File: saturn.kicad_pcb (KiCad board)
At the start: 4 copper layers, 100 x 66 mm, 101 parts, among them J1 Conn_01x04_Pin, J10 Conn_01x04, J11 USB_B_Micro, J12 USB_C_Receptacle_USB2.0, J13 ZX-XH2.54-3PWT, J14 Conn_01x04_Pin, J2 PMOD3_FULL, J3 Conn_01x06, J4 Conn_01x06, J6 ZX-XH2.54-10PWT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

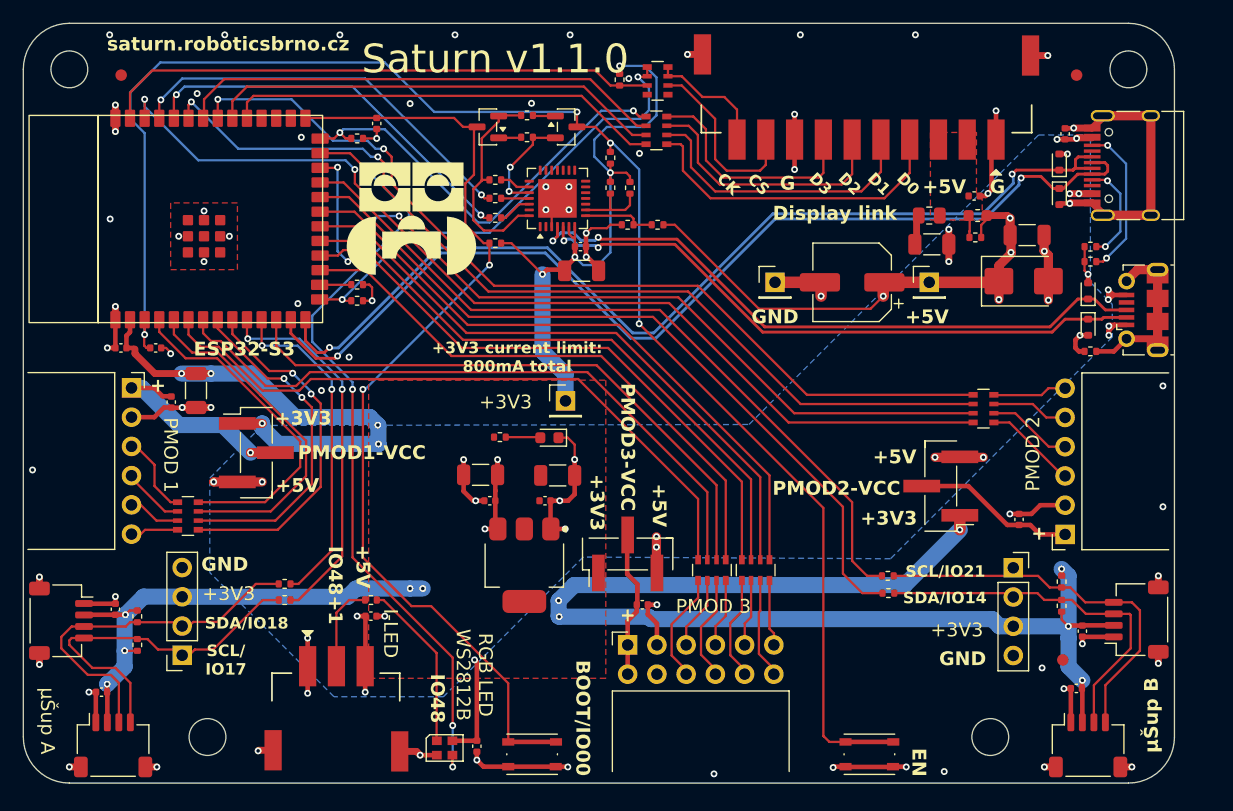
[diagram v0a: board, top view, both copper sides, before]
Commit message: Tune silkscreen, enlarge SMT switch pads
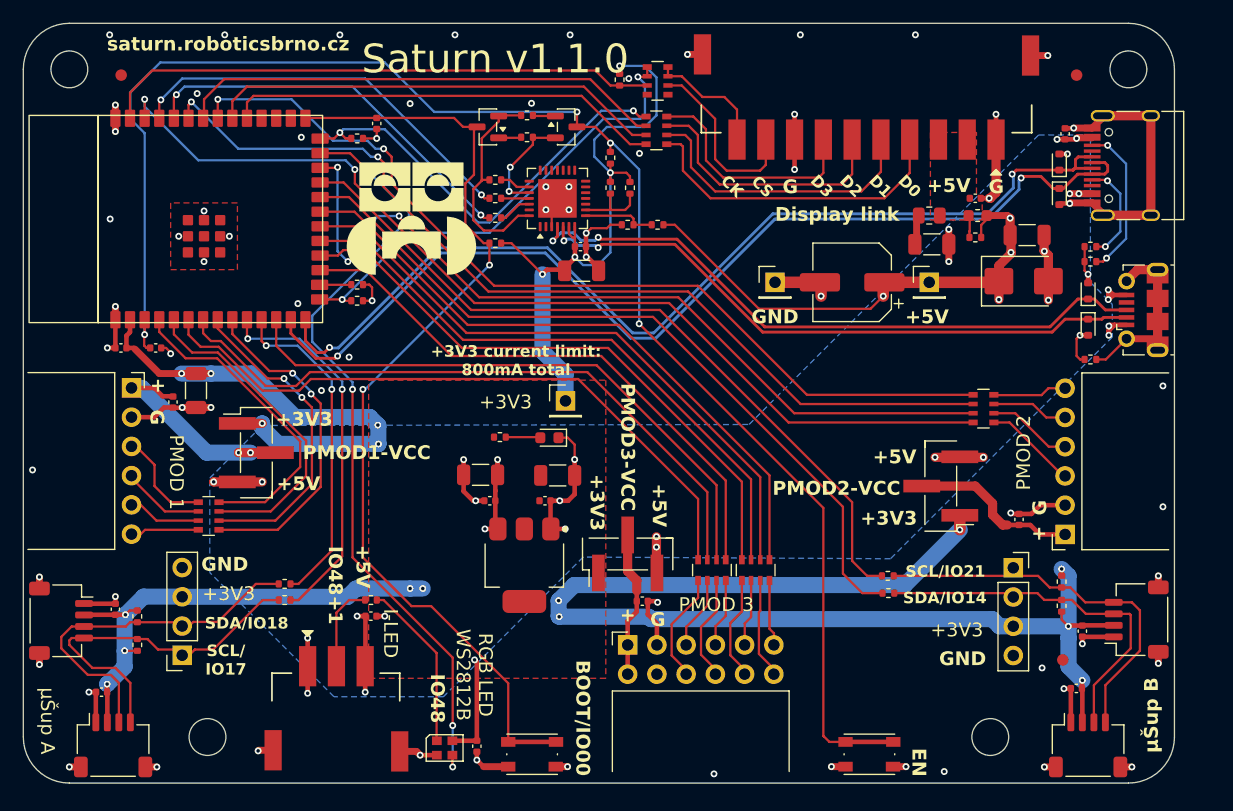
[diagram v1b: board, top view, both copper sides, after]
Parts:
- SW2, SW3: footprint Button_Switch_SMD:SW_Push_1P1T_NO_Vertical_Wuerth_434133025816 -> Switch_SMT:SW_SMD_LargePads
- moved RN1 1.80 mm to (61.1, 98.8)
- moved R71 0.70 mm to (137.7, 85.2)
- moved C9 0.31 mm to (98.8, 106.2)
- moved C21 0.22 mm to (127.7, 71.2)
- moved C23 0.15 mm to (58.0, 88.9)
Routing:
- net GND: track 168.3 -> 161.1 mm
- net Net-(J3-Pin_3): track 5.41 -> 7.21 mm
- net Net-(J3-Pin_2): track 4.57 -> 6.37 mm
- net Net-(J3-Pin_1): track 4.16 -> 5.96 mm
- net Net-(J3-Pin_4): track 7.09 -> 8.89 mm
- net /PMOD1_IO2: track 29.7 -> 27.9 mm
- net /PMOD1_IO1: track 30.9 -> 29.1 mm
- net /PMOD1_IO4: track 29.6 -> 27.8 mm
- net /PMOD1_IO3: track 30.3 -> 28.5 mm
- net Net-(J3-Pin_6): track 18.6 -> 19.8 mm, vias 1 -> 2
- net Net-(J4-Pin_6): track 14.2 -> 14.8 mm
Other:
- board text added: "ESP32-S3-WROOM-1-N16R8 Octal PSRAM"
- board text removed: "ESP32-S3"

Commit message: Use 0805 10u capacitors (cheaper)
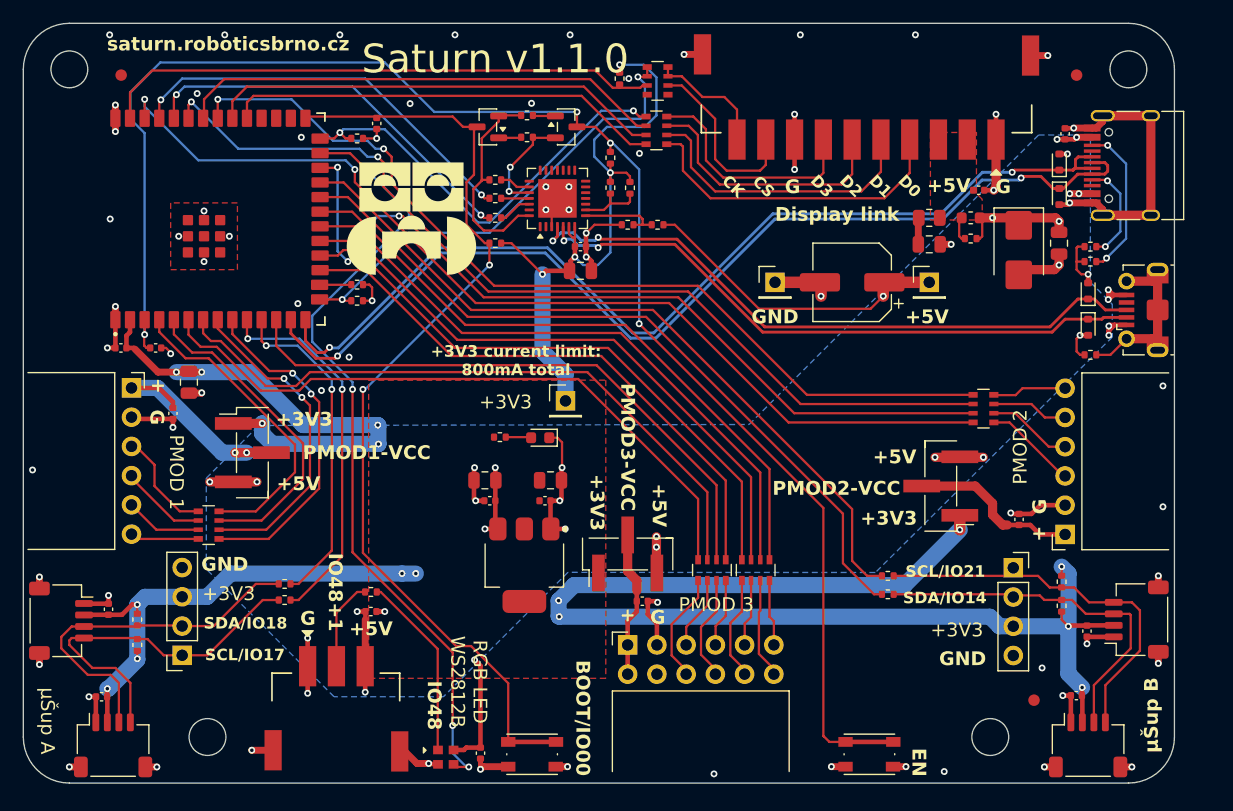
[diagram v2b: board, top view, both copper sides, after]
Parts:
- C1, C24, C3, C4, C5, C6: footprint Capacitor_SMD:C_1206_3216Metric -> Capacitor_SMD:C_0805_2012Metric
- J11: footprint Connector_USB:USB_Micro-B_Molex-105017-0001 -> USB_Conn:USB_Micro-B_XNJ-073_With_THR_Paste
- J12: footprint Connector_USB:USB_C_Receptacle_HRO_TYPE-C-31-M-12 -> USB_Conn:USB_C_Receptacle_HRO_TYPE-C-31-M-12_With_THR_Paste
- U1: footprint RKL-ESP:ESP32-S3-WROOM -> ESP32-WROOM:ESP32-S3-WROOM
- U9: footprint LED_SMD:LED_WS2812B-2020_PLCC4_2.0x2.0mm -> XL-2020RGBC-WS2812B:LED_WS2812B-2020_PLCC4_2.0x2.0mm
- moved FID3 4.30 mm to (132.8, 114.8)
- moved C4 2.86 mm to (135.0, 75.1), turned to -90 degrees
- moved D5 2.73 mm to (131.5, 75.7), turned to -90 degrees
- moved C23 0.99 mm to (58.0, 89.9)
- moved C1 0.95 mm to (59.4, 87.2)
- moved U9 0.81 mm to (81.7, 119.8)
- moved D2 0.80 mm to (89.9, 92.0)
- moved RN1 0.79 mm to (61.1, 99.6)
- moved C21 0.76 mm to (128.0, 70.5)
- moved C5 0.75 mm to (90.8, 95.7)
- moved R33 0.70 mm to (75.2, 105.4)
- moved C16 0.68 mm to (84.7, 119.4)
- moved FB1 0.63 mm to (127.3, 72.9)
- moved C13 0.62 mm to (136.5, 114.4)
- moved C6 0.61 mm to (85.1, 95.7)
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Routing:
- net +5V: track 89.8 -> 83.4 mm, vias 21 -> 20
- net GND: track 161.1 -> 155.3 mm, vias 88 -> 86
- net Net-(U9-DOUT): track 14.7 -> 16.4 mm
- net +3V3: track 248.4 -> 249.8 mm
- net /SMART_LEDS: track 67.6 -> 68.7 mm
- net Net-(J11-Shield): track 16.3 -> 15.4 mm
- net /I2CB_SDA: track 66.5 -> 65.6 mm
- net /USBMAIN_D+: track 86.8 -> 85.9 mm
- net Net-(D2-A): track 3.02 -> 2.22 mm
- net Net-(U3-VBUS): track 6.38 -> 7.15 mm
- net Net-(U3-~{RST}): track 6.44 -> 5.71 mm
- net Net-(J3-Pin_6): track 19.8 -> 20.4 mm
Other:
- board text removed: "SCL/ IO17"

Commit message: Use AMS1117-3.3 LDO (cheaper)
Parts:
- U2: value SGM2212-3.3XKC3G -> AMS1117-3.3
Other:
- board text added: "+3V3 current limit: 1A total"
- board text removed: "+3V3 current limit: 800mA total"
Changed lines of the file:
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@@
 			)
 		)
-		(property "Value" "SGM2212-3.3XKC3G"
+		(property "Value" "AMS1117-3.3"
 			(at 0.0625 -6.25 90)
 			(layer "F.Fab")
@@
 			)
 		)
-		(property "LCSC" "C3294699"
+		(property "LCSC" "C6186"
 			(at 0 0 270)
 			(unlocked yes)
@@
 		(layer "Edge.Cuts")
 	)
-	(gr_text "+3V3 current limit:\n800mA total"
+	(gr_text "+3V3 current limit:\n1A total"
 		(at 87.8 85.3 0)
 		(layer "F.SilkS")
@@
 	)
 	(gr_text "Display link"
-		(at 115.7 72.6 0)
+		(at 115.6 72.9 0)
 		(layer "F.SilkS")
 		(effects

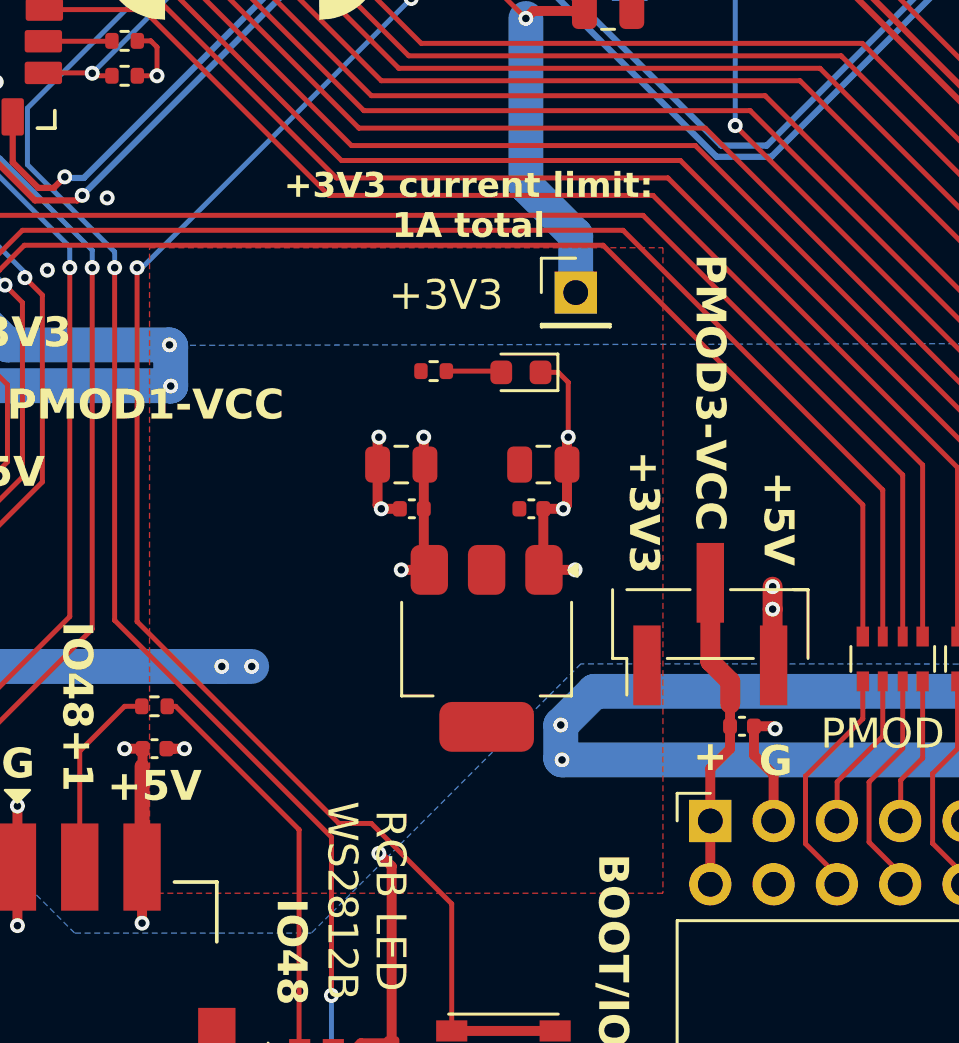
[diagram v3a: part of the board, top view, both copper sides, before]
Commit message: Add LDO output cap series resistance
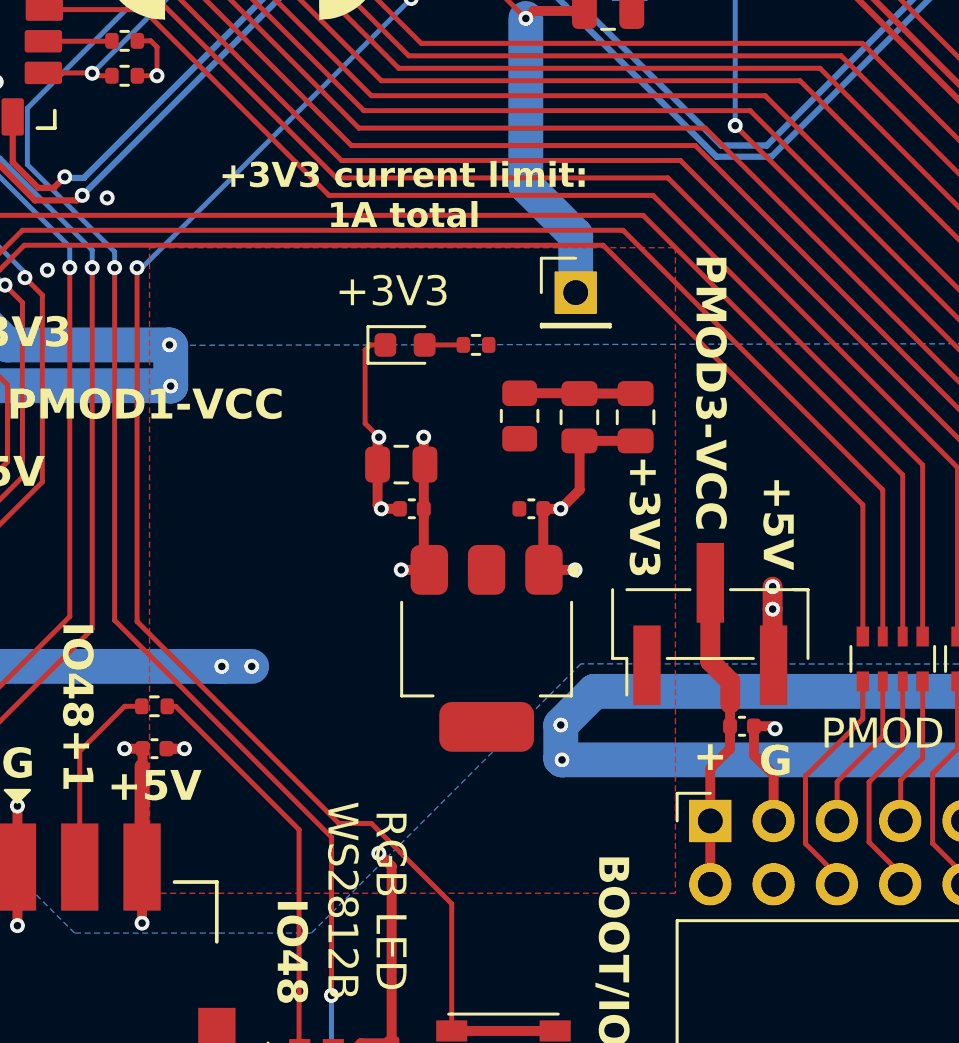
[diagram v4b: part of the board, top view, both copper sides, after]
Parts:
- added C25: 10u, Capacitor_SMD:C_0805_2012Metric, F.Cu at (94.5, 93.8)
- added R20: 4R7, Resistor_SMD:R_0805_2012Metric, F.Cu at (89.8, 93.8)
- moved D2 4.78 mm to (85.2, 90.9), turned to 0 degrees
- moved C5 2.39 mm to (92.2, 93.8), turned to -90 degrees
- moved R5 2.00 mm to (88.1, 90.9), turned to 180 degrees
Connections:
- C5 pad 1: +3V3 -> Net-(C25-Pad1)
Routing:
- net Net-(C25-Pad1): track 0.00 -> 4.66 mm
- net GND: track 155.3 -> 158.7 mm, vias 86 -> 85
- net Net-(D2-A): track 2.22 -> 1.55 mm

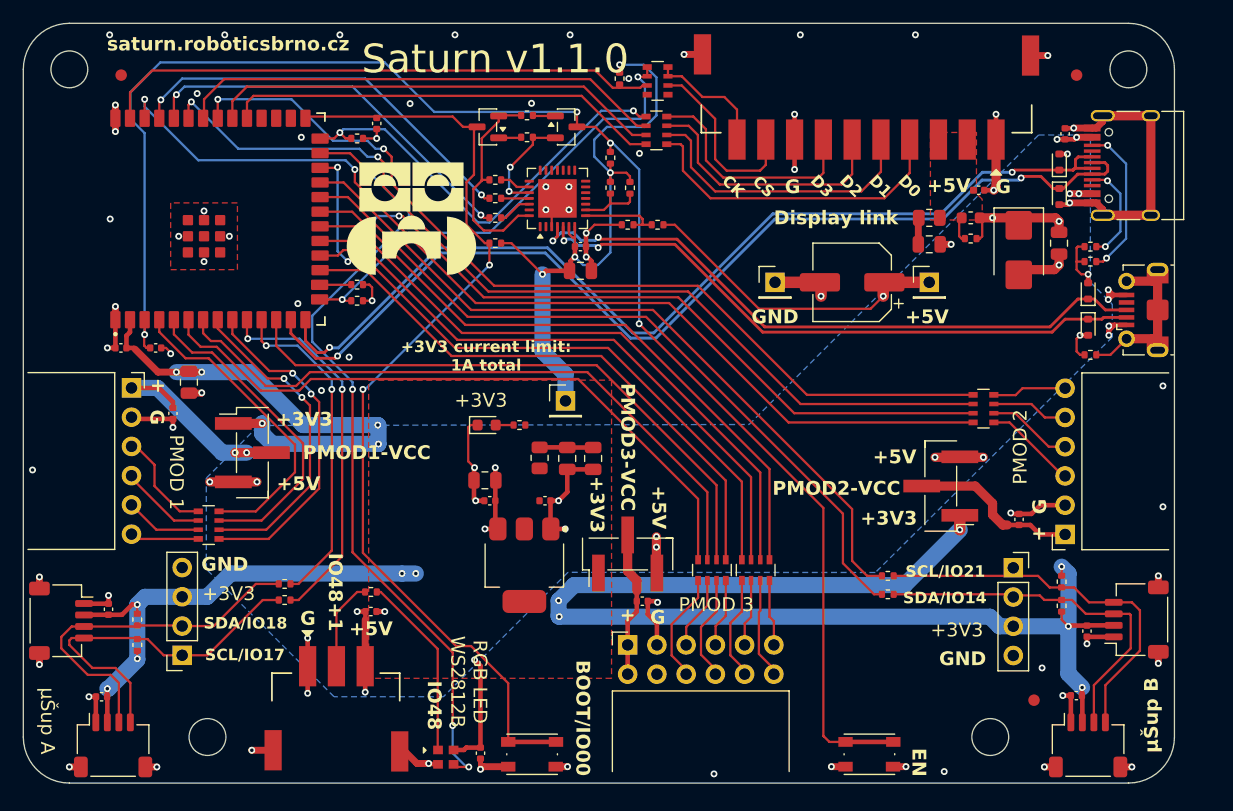
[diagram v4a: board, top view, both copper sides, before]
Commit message: Separate LED Strip to IO46 with level shift, tune layout
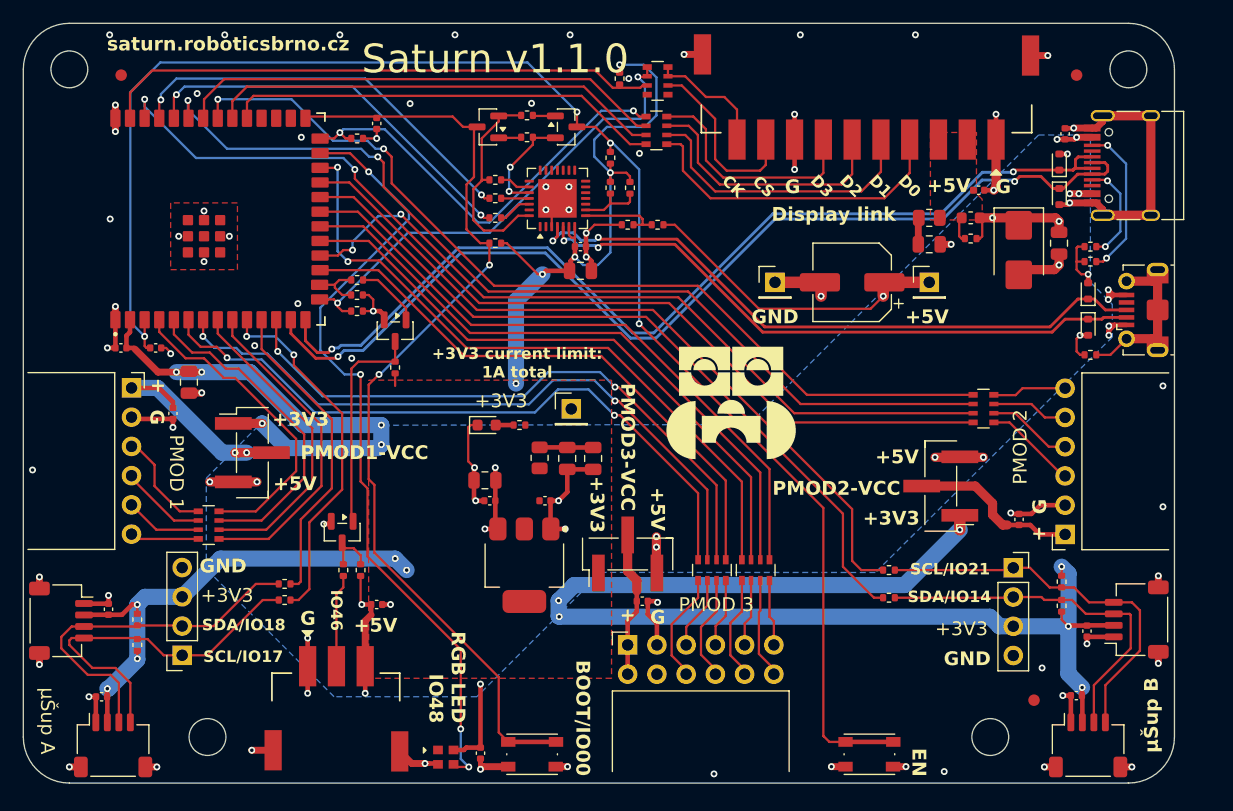
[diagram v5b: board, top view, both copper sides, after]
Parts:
- added Q5: Q_NPN_BEC, Package_TO_SOT_SMD:SOT-23, F.Cu at (77.3, 82.7)
- added Q6: Q_NPN_BEC, Package_TO_SOT_SMD:SOT-23, F.Cu at (72.7, 100.2)
- added R21: 2k, Resistor_SMD:R_0402_1005Metric, F.Cu at (74.3, 103.5)
- added R22: 10k, Resistor_SMD:R_0402_1005Metric, F.Cu at (74.0, 78.3)
- added R72: 5k1, Resistor_SMD:R_0402_1005Metric, F.Cu at (77.3, 85.9)
- moved R33 3.06 mm to (72.8, 103.5), turned to -90 degrees
- moved R14 0.90 mm to (74.0, 81.0)
- moved R16 0.90 mm to (74.0, 79.6)
- moved TP3 0.86 mm to (92.6, 89.5)
- moved C10 0.79 mm to (75.7, 106.5)
- moved R4 0.51 mm to (120.2, 103.5)
- moved R6 0.32 mm to (120.2, 105.9)
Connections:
- net /SMART_LEDS renamed /SMART_LED
- net Net-(U1-IO46-PD) renamed /SMART_LEDS_STRIP
- R33 pad 1: Net-(U9-DOUT) -> Net-(Q6-C)
- U9 pad 1: Net-(U9-DOUT) -> unconnected-(U9-DOUT-Pad1)
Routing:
- net Net-(Q5-C): track 0.00 -> 19.1 mm
- net Net-(U9-DOUT): track 16.4 -> 0.00 mm
- net Net-(Q5-B): track 0.00 -> 5.77 mm
- net Net-(Q6-C): track 0.00 -> 4.82 mm
- net GND: track 158.7 -> 161.2 mm, vias 85 -> 86
- net /SMART_LEDS_STRIP: track 2.76 -> 4.87 mm
- net /PMOD3_IO9: track 52.0 -> 54.0 mm, vias 0 -> 2
- net /I2CA_SDA: track 29.0 -> 27.4 mm, vias 2 -> 0
- net +5V: track 83.4 -> 84.6 mm
- net /I2CA_SCL: track 32.7 -> 31.5 mm
- net /PMOD3_IO10: track 57.6 -> 58.7 mm, vias 0 -> 2
- net /DISPLAY_CLK: track 40.9 -> 42.0 mm
- net /PMOD3_IO4: track 57.6 -> 58.6 mm, vias 0 -> 2
- net /GPIO0/BOOT: track 85.2 -> 84.2 mm
- net /PMOD1_IO1: track 29.4 -> 28.5 mm, vias 2 -> 0
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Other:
- board text added: "IO46"
- board text added: "RGB LED IO48"
- board text added: "RGB Strip WS2812B LEDs"
- board text removed: "I-LED"
- board text removed: "IO48"
- board text removed: "IO48+1"

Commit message: Tune layout, POS corrections, kik.json
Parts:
- added T1: Tab, kikit:Tab, F.Cu at (61.0, 55.5)
- added T2: Tab, kikit:Tab, F.Cu at (129.0, 55.5)
- added T3: Tab, kikit:Tab, F.Cu at (129.0, 123.0)
- added T4: Tab, kikit:Tab, F.Cu at (61.0, 122.5)
- moved J6 1.10 mm to (118.2, 62.8)
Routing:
- net unconnected-(U9-DOUT-Pad1): track 0.30 -> 1.60 mm
- net +5V: track 84.6 -> 84.0 mm
- net GND: track 161.2 -> 160.8 mm, vias 86 -> 83

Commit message: Ignore -bridged-wtf-DRC-thing-, tune Makefile
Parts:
- moved C19 0.05 mm to (135.5, 65.7)
- moved J12 0.05 mm to (141.9, 68.4)
